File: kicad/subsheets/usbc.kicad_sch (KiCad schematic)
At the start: 12 parts

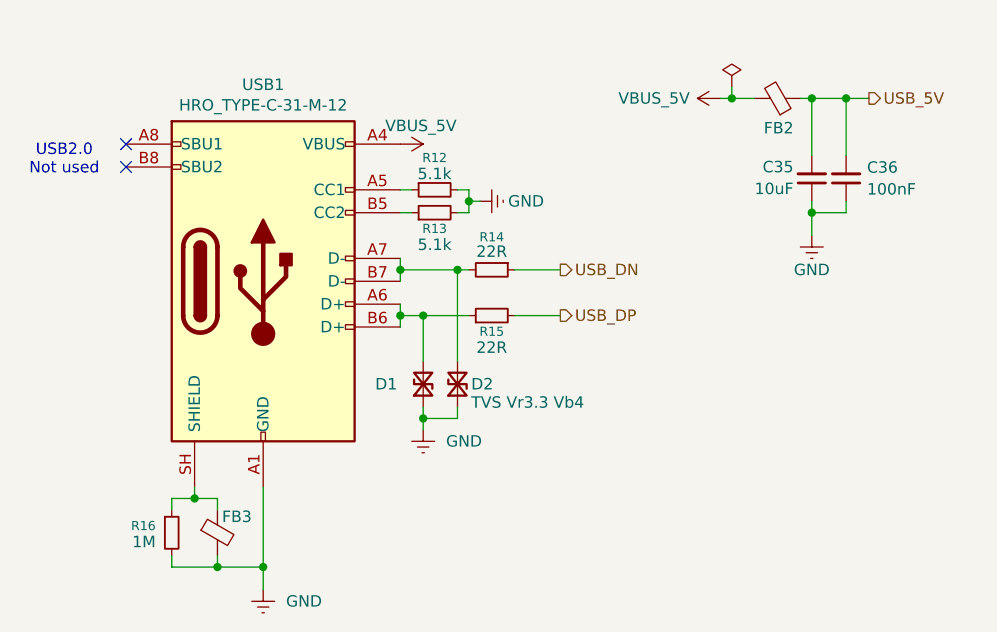
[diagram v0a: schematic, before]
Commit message: PCB before switching STM32
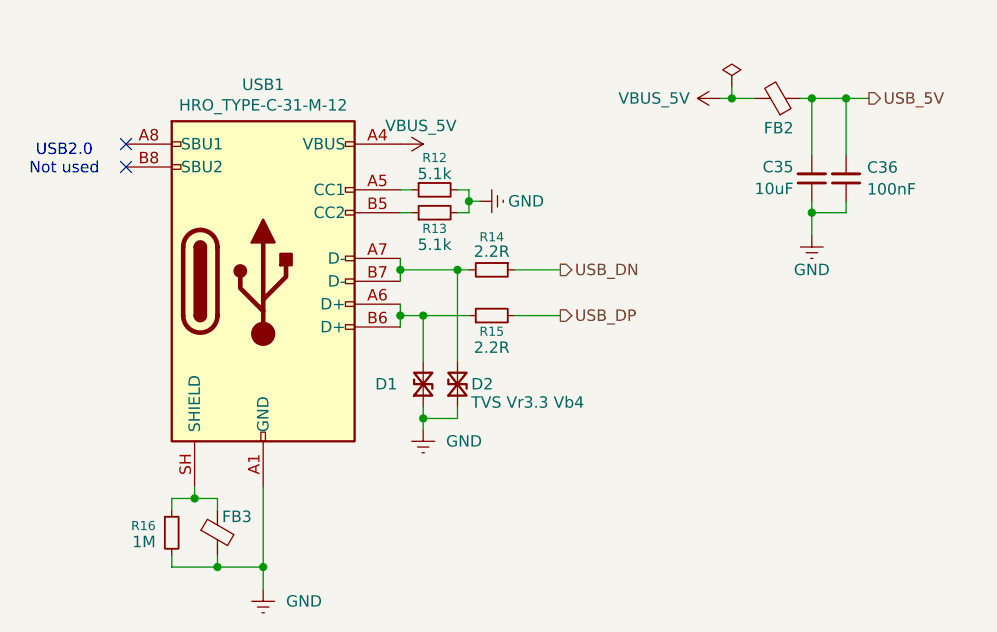
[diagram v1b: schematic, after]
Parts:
- R14, R15: value 22R -> 2.2R
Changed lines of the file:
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@@
 			)
 		)
-		(property "Value" "22R"
+		(property "Value" "2.2R"
 			(at 156.21 100.076 90)
 			(show_name no)
@@
 			)
 		)
-		(property "Value" "22R"
+		(property "Value" "2.2R"
 			(at 156.21 89.408 90)
 			(show_name no)

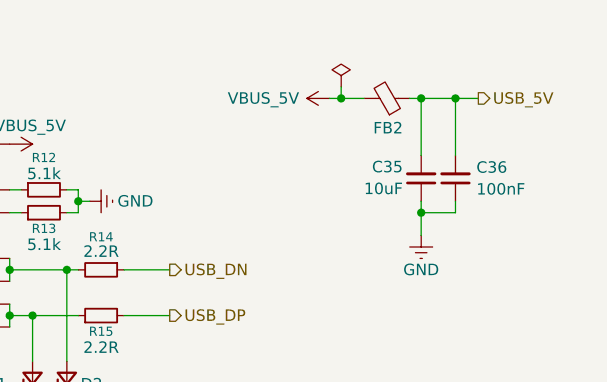
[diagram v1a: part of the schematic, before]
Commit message: Add missing passives and microphone
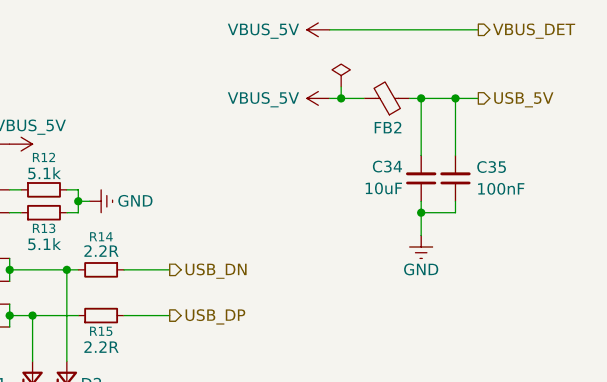
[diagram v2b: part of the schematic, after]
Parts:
- renumbered C35 to C34, C36 to C35
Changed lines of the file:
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@@
 	(wire
 		(pts
+			(xy 198.12 64.77) (xy 181.61 64.77)
+		)
+		(stroke
+			(width 0)
+			(type default)
+		)
+	)
+	(wire
+		(pts
 			(xy 191.77 72.39) (xy 195.58 72.39)
 		)
@@
 		)
 	)
+	(hierarchical_label "VBUS_DET"
+		(shape output)
+		(at 198.12 64.77 0)
+		(effects
+			(font
+				(size 1.27 1.27)
+			)
+			(justify left)
+		)
+	)
 	(symbol
 		(lib_id "a3-srad-camera-v2:GND")
@@
 		(dnp no)
 		(fields_autoplaced yes)
-		(property "Reference" "#PWR037"
+		(property "Reference" "#PWR036"
 			(at 148.59 115.57 0)
 			(hide yes)
@@
 			(project "a3-srad-camera-v2"
 				(path "/c4ff1aa6-4aa7-4de3-a597-83271e910ec4/8a49aa55-9ab2-4128-b069-6e62671c968c"
-					(reference "#PWR037")
+					(reference "#PWR036")
 					(unit 1)
 				)
@@
 		(dnp no)
 		(fields_autoplaced yes)
-		(property "Reference" "C36"
+		(property "Reference" "C35"
 			(at 197.9041 80.0614 0)
 			(show_name no)
@@
 			(project "a3-srad-camera-v2"
 				(path "/c4ff1aa6-4aa7-4de3-a597-83271e910ec4/8a49aa55-9ab2-4128-b069-6e62671c968c"
-					(reference "C36")
+					(reference "C35")
 					(unit 1)
 				)
@@
 		(dnp no)
 		(fields_autoplaced yes)
-		(property "Reference" "#PWR038"
+		(property "Reference" "#PWR037"
 			(at 130.81 133.35 0)
 			(hide yes)
@@
 			(project "a3-srad-camera-v2"
 				(path "/c4ff1aa6-4aa7-4de3-a597-83271e910ec4/8a49aa55-9ab2-4128-b069-6e62671c968c"
-					(reference "#PWR038")
+					(reference "#PWR037")
 					(unit 1)
 				)
@@
 		(dnp no)
 		(fields_autoplaced yes)
-		(property "Reference" "#PWR033"
+		(property "Reference" "#PWR032"
 			(at 185.42 72.39 0)
 			(hide yes)
@@
 			(project "a3-srad-camera-v2"
 				(path "/c4ff1aa6-4aa7-4de3-a597-83271e910ec4/8a49aa55-9ab2-4128-b069-6e62671c968c"
-					(reference "#PWR033")
+					(reference "#PWR032")
 					(unit 1)
 				)
@@
 		(in_pos_files yes)
 		(dnp no)
-		(property "Reference" "#PWR035"
+		(property "Reference" "#PWR034"
 			(at 161.29 83.82 0)
 			(hide yes)
@@
 			(project "a3-srad-camera-v2"
 				(path "/c4ff1aa6-4aa7-4de3-a597-83271e910ec4/8a49aa55-9ab2-4128-b069-6e62671c968c"
-					(reference "#PWR035")
+					(reference "#PWR034")
 					(unit 1)
 				)
@@
 		(in_pos_files yes)
 		(dnp no)
-		(property "Reference" "#PWR036"
+		(property "Reference" "#PWR035"
 			(at 191.77 93.98 0)
 			(hide yes)
@@
 			(project "a3-srad-camera-v2"
 				(path "/c4ff1aa6-4aa7-4de3-a597-83271e910ec4/8a49aa55-9ab2-4128-b069-6e62671c968c"
-					(reference "#PWR036")
+					(reference "#PWR035")
 					(unit 1)
 				)
@@
 		(in_pos_files yes)
 		(dnp no)
-		(property "Reference" "#PWR034"
+		(property "Reference" "#PWR033"
 			(at 142.24 77.47 0)
 			(hide yes)
@@
 			(project "a3-srad-camera-v2"
 				(path "/c4ff1aa6-4aa7-4de3-a597-83271e910ec4/8a49aa55-9ab2-4128-b069-6e62671c968c"
-					(reference "#PWR034")
+					(reference "#PWR033")
+					(unit 1)
+				)
+			)
+		)
+	)
+	(symbol
+		(lib_id "power:VCC")
+		(at 181.61 64.77 90)
+		(mirror x)
+		(unit 1)
+		(body_style 1)
+		(exclude_from_sim no)
+		(in_bom yes)
+		(on_board yes)
+		(in_pos_files yes)
+		(dnp no)
+		(fields_autoplaced yes)
+		(property "Reference" "#PWR068"
+			(at 185.42 64.77 0)
+			(hide yes)
+			(show_name no)
+			(do_not_autoplace no)
+			(effects
+				(font
+					(size 1.27 1.27)
+				)
+			)
+		)
+		(property "Value" "VBUS_5V"
+			(at 174.2417 64.77 90)
+			(show_name no)
+			(do_not_autoplace no)
+			(effects
+				(font
+					(size 1.27 1.27)
+				)
+			)
+		)
+		(property "Footprint" ""
+			(at 181.61 64.77 0)
+			(hide yes)
+			(show_name no)
+			(do_not_autoplace no)
+			(effects
+				(font
+					(size 1.27 1.27)
+				)
+			)
+		)
+		(property "Datasheet" ""
+			(at 181.61 64.77 0)
+			(hide yes)
+			(show_name no)
+			(do_not_autoplace no)
+			(effects
+				(font
+					(size 1.27 1.27)
+				)
+			)
+		)
+		(property "Description" "Power symbol creates a global label with name \"VCC\""
+			(at 181.61 64.77 0)
+			(hide yes)
+			(show_name no)
+			(do_not_autoplace no)
+			(effects
+				(font
+					(size 1.27 1.27)
+				)
+			)
+		)
+		(pin "1"
+		)
+		(instances
+			(project "a3-srad-camera-v2"
+				(path "/c4ff1aa6-4aa7-4de3-a597-83271e910ec4/8a49aa55-9ab2-4128-b069-6e62671c968c"
+					(reference "#PWR068")
 					(unit 1)
 				)
@@
 		(in_pos_files yes)
 		(dnp no)
-		(property "Reference" "C35"
+		(property "Reference" "C34"
 			(at 189.738 80.01 0)
 			(show_name no)
@@
 			(project "a3-srad-camera-v2"
 				(path "/c4ff1aa6-4aa7-4de3-a597-83271e910ec4/8a49aa55-9ab2-4128-b069-6e62671c968c"
-					(reference "C35")
+					(reference "C34")
 					(unit 1)
 				)

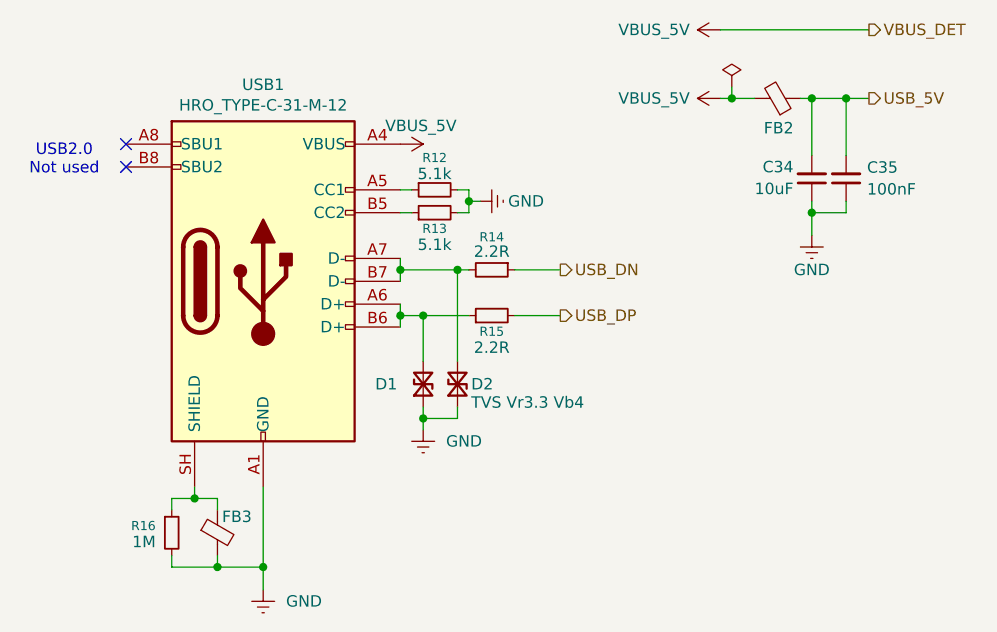
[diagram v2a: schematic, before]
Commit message: Footprint + silkscreen corrections
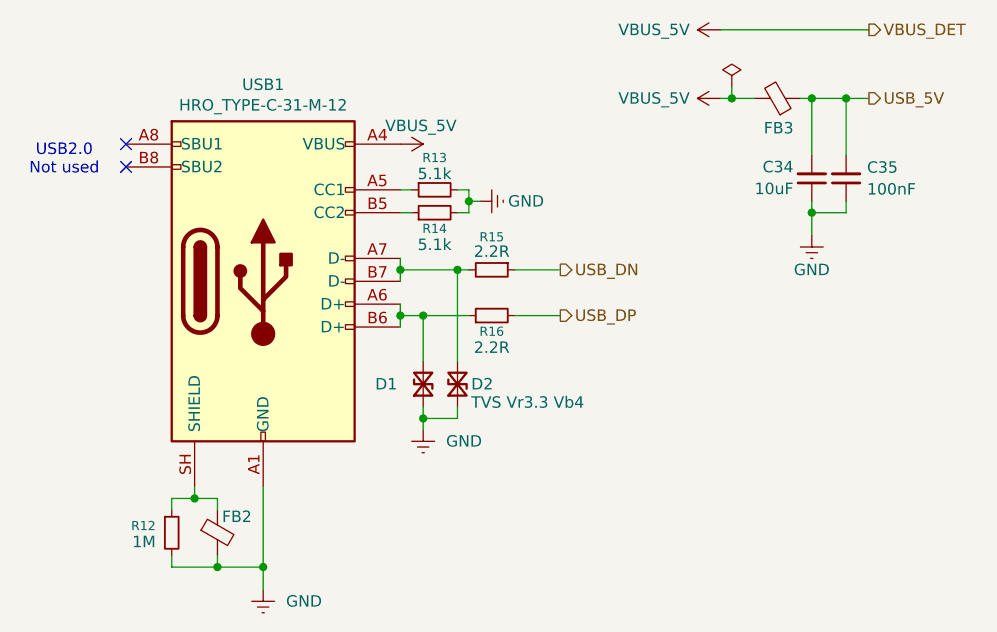
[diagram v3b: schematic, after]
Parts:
- C34, C35, USB1: now left out of the parts list
- D1, D2: footprint Diode_SMD:D_SOD-123F -> Diode_SMD:D_SOD-323; now left out of the parts list
- FB2: renamed from FB3; now left out of the parts list
- FB3: renamed from FB2; now left out of the parts list
- R12: renamed from R16; now left out of the parts list
- R13: renamed from R12; now left out of the parts list
- R14: renamed from R13; now left out of the parts list
- R15: renamed from R14; now left out of the parts list
- R16: renamed from R15; now left out of the parts list

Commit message: Minor kicad changes
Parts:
- C34, C35, D1, D2, FB3, R15, R16: now in the parts list
- FB2, R12, R13, R14, USB1: BOARD_SIDE (none) -> Front; now in the parts list
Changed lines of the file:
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@@
 		(body_style 1)
 		(exclude_from_sim no)
-		(in_bom no)
+		(in_bom yes)
 		(on_board yes)
 		(in_pos_files yes)
@@
 			)
 		)
+		(property "BOARD_SIDE" "Front"
+			(at 149.86 82.55 90)
+			(hide yes)
+			(show_name no)
+			(do_not_autoplace no)
+			(effects
+				(font
+					(size 1.27 1.27)
+				)
+			)
+		)
 		(pin "1"
 		)
@@
 		(body_style 1)
 		(exclude_from_sim no)
-		(in_bom no)
+		(in_bom yes)
 		(on_board yes)
 		(in_pos_files yes)
@@
 			)
 		)
+		(property "BOARD_SIDE" ""
+			(at 156.21 96.52 90)
+			(hide yes)
+			(show_name no)
+			(do_not_autoplace no)
+			(effects
+				(font
+					(size 1.27 1.27)
+				)
+			)
+		)
 		(pin "1"
 		)
@@
 		(body_style 1)
 		(exclude_from_sim no)
-		(in_bom no)
+		(in_bom yes)
 		(on_board yes)
 		(in_pos_files yes)
@@
 			)
 		)
+		(property "BOARD_SIDE" "Front"
+			(at 120.65 120.65 0)
+			(hide yes)
+			(show_name no)
+			(do_not_autoplace no)
+			(effects
+				(font
+					(size 1.27 1.27)
+				)
+			)
+		)
 		(pin "1"
 		)
@@
 		(body_style 1)
 		(exclude_from_sim no)
-		(in_bom no)
+		(in_bom yes)
 		(on_board yes)
 		(in_pos_files yes)
@@
 			)
 		)
+		(property "BOARD_SIDE" ""
+			(at 195.58 81.28 0)
+			(hide yes)
+			(show_name no)
+			(do_not_autoplace no)
+			(effects
+				(font
+					(size 1.27 1.27)
+				)
+			)
+		)
 		(pin "2"
 		)
@@
 		(body_style 1)
 		(exclude_from_sim no)
-		(in_bom no)
+		(in_bom yes)
 		(on_board yes)
 		(in_pos_files yes)
@@
 			)
 		)
+		(property "BOARD_SIDE" "Front"
+			(at 125.73 120.65 0)
+			(hide yes)
+			(show_name no)
+			(do_not_autoplace no)
+			(effects
+				(font
+					(size 1.27 1.27)
+				)
+			)
+		)
 		(pin "1"
 		)
@@
 		(body_style 1)
 		(exclude_from_sim no)
-		(in_bom no)
+		(in_bom yes)
 		(on_board yes)
 		(in_pos_files yes)
@@
 			)
 		)
+		(property "BOARD_SIDE" ""
+			(at 187.96 72.39 90)
+			(hide yes)
+			(show_name no)
+			(do_not_autoplace no)
+			(effects
+				(font
+					(size 1.27 1.27)
+				)
+			)
+		)
 		(pin "1"
 		)
@@
 		(body_style 1)
 		(exclude_from_sim no)
-		(in_bom no)
+		(in_bom yes)
 		(on_board yes)
 		(in_pos_files yes)
@@
 			)
 		)
+		(property "BOARD_SIDE" "Front"
+			(at 149.86 85.09 90)
+			(hide yes)
+			(show_name no)
+			(do_not_autoplace no)
+			(effects
+				(font
+					(size 1.27 1.27)
+				)
+			)
+		)
 		(pin "1"
 		)
@@
 		(body_style 1)
 		(exclude_from_sim no)
-		(in_bom no)
+		(in_bom yes)
 		(on_board yes)
 		(in_pos_files yes)
@@
 			)
 		)
+		(property "BOARD_SIDE" "Front"
+			(at 130.81 92.71 0)
+			(hide yes)
+			(show_name no)
+			(do_not_autoplace no)
+			(effects
+				(font
+					(size 1.27 1.27)
+				)
+			)
+		)
 		(pin "B4"
 		)
@@
 		(body_style 1)
 		(exclude_from_sim no)
-		(in_bom no)
+		(in_bom yes)
 		(on_board yes)
 		(in_pos_files yes)
@@
 			)
 		)
+		(property "BOARD_SIDE" ""
+			(at 156.21 91.44 90)
+			(hide yes)
+			(show_name no)
+			(do_not_autoplace no)
+			(effects
+				(font
+					(size 1.27 1.27)
+				)
+			)
+		)
 		(pin "1"
 		)
@@
 		(body_style 1)
 		(exclude_from_sim no)
-		(in_bom no)
+		(in_bom yes)
 		(on_board yes)
 		(in_pos_files yes)
@@
 			)
 		)
+		(property "BOARD_SIDE" ""
+			(at 152.4 104.14 90)
+			(hide yes)
+			(show_name no)
+			(do_not_autoplace no)
+			(effects
+				(font
+					(size 1.27 1.27)
+				)
+			)
+		)
 		(pin "2"
 		)
@@
 		(body_style 1)
 		(exclude_from_sim no)
-		(in_bom no)
+		(in_bom yes)
 		(on_board yes)
 		(in_pos_files yes)
@@
 			)
 		)
+		(property "BOARD_SIDE" ""
+			(at 191.77 81.28 0)
+			(hide yes)
+			(show_name no)
+			(do_not_autoplace no)
+			(effects
+				(font
+					(size 1.27 1.27)
+				)
+			)
+		)
 		(pin "2"
 		)
@@
 		(body_style 1)
 		(exclude_from_sim no)
-		(in_bom no)
+		(in_bom yes)
 		(on_board yes)
 		(in_pos_files yes)
@@
 			(at 148.59 104.14 90)
 			(hide yes)
+			(show_name no)
+			(do_not_autoplace no)
+			(effects
+				(font
+					(size 1.27 1.27)
+				)
+			)
+		)
+		(property "BOARD_SIDE" ""
+			(at 148.59 104.14 90)
+			(hide yes)
